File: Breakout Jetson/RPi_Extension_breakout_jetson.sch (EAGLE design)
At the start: 9 parts, among them U1 CD74HC137, U2 CD74HC137

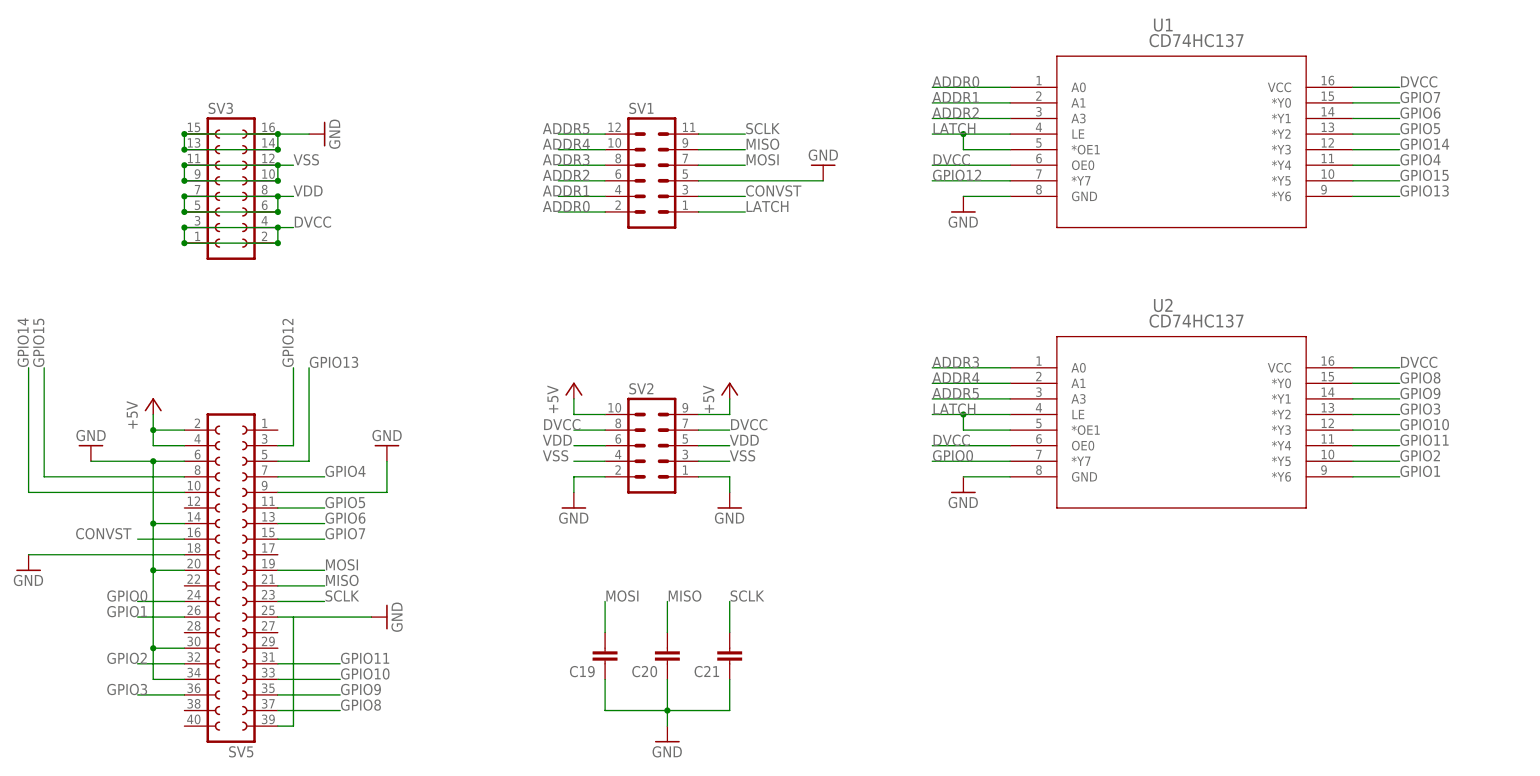
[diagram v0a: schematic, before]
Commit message: changed used component to one 1 to 16 multiplexer on basic jetson tx1 board
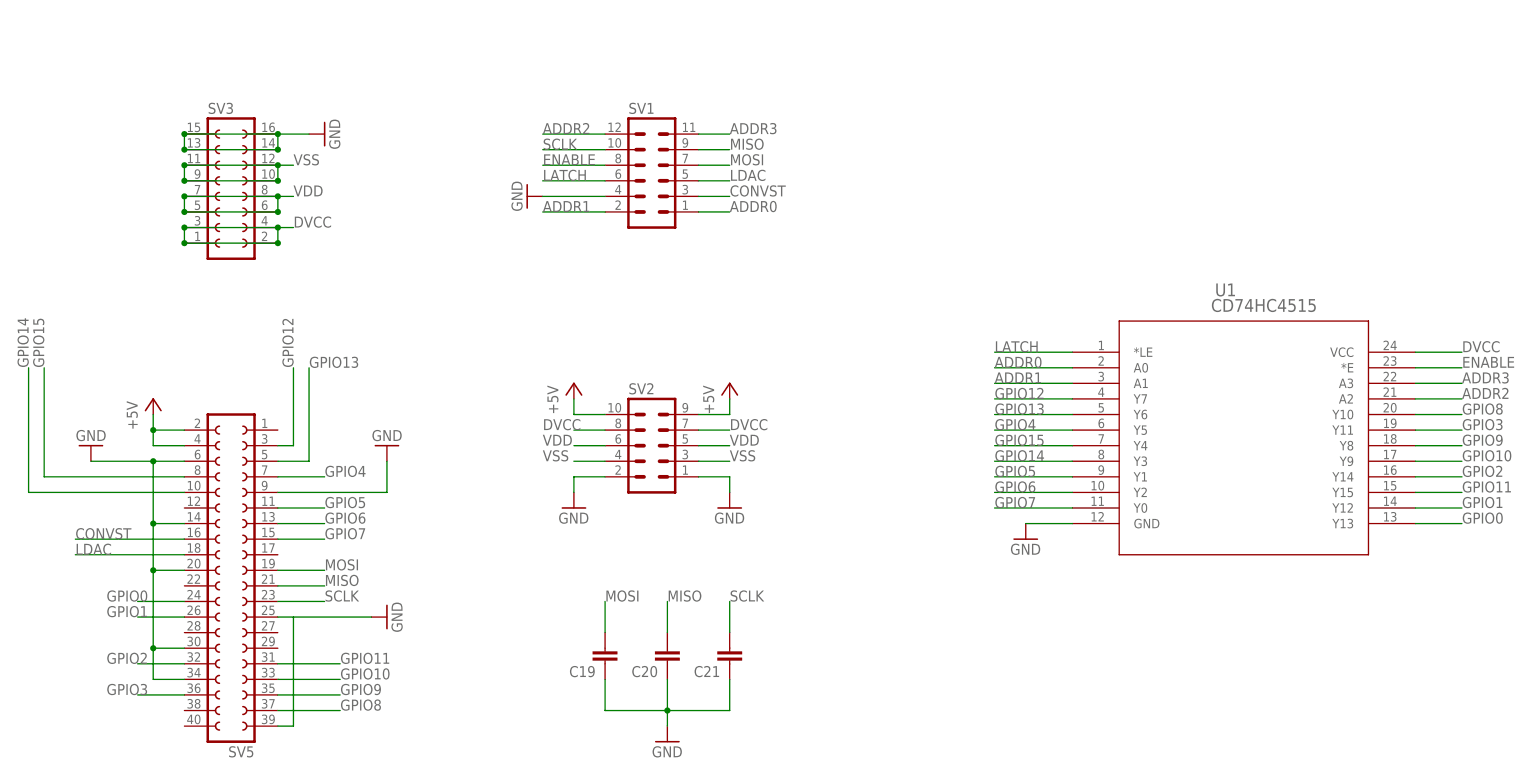
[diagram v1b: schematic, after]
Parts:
- removed U2: CD74HC137, CD74HC137:CD74HC137_PW_16
- U1: value CD74HC137 -> CD74HC4515; device CD74HC137:CD74HC137_PW_16 -> CD74HC4515:CD74HC4515_DW_24
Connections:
- removed net ADDR4: SV1.10, U2.A1
- removed net ADDR5: SV1.12, U2.A3
- new net ENABLE: SV1.8, U1.*E
- new net LDAC: SV1.5, SV5.18
- net ADDR0: now also SV1.1; no longer SV1.2
- net ADDR1: now also SV1.2; no longer SV1.4
- net ADDR2: now also SV1.12, U1.A2; no longer SV1.6, U1.A3
- net ADDR3: now also SV1.11, U1.A3; no longer SV1.8, U2.A0
- net DVCC: no longer U1.OE0, U2.OE0, U2.VCC
- net GND: now also SV1.4; no longer SV1.5, SV5.18, U2.GND
- net GPIO0: now also U1.Y13; no longer U2.*Y7
- net GPIO1: now also U1.Y12; no longer U2.*Y6
- net GPIO10: now also U1.Y9; no longer U2.*Y3
- net GPIO11: now also U1.Y15; no longer U2.*Y4
- net GPIO12: now also U1.Y7; no longer U1.*Y7
- net GPIO13: now also U1.Y6; no longer U1.*Y6
- net GPIO14: now also U1.Y3; no longer U1.*Y3
- net GPIO15: now also U1.Y4; no longer U1.*Y5
- net GPIO2: now also U1.Y14; no longer U2.*Y5
- net GPIO3: now also U1.Y11; no longer U2.*Y2
- net GPIO4: now also U1.Y5; no longer U1.*Y4
- net GPIO5: now also U1.Y1; no longer U1.*Y2
- net GPIO6: now also U1.Y2; no longer U1.*Y1
- net GPIO7: now also U1.Y0; no longer U1.*Y0
- net GPIO8: now also U1.Y10; no longer U2.*Y0
- net GPIO9: now also U1.Y8; no longer U2.*Y1
- net LATCH: now also SV1.6, U1.*LE; no longer SV1.1, U1.*OE1, U1.LE, U2.*OE1, U2.LE
- net SCLK: now also SV1.10; no longer SV1.11
